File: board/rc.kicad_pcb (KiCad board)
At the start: 2 copper layers, 74 x 47.3 mm, 42 parts, among them IC1 A3909GLNTR-T, J1 Conn_01x24, J2 Conn_01x06, Q1 Q_NPN_BEC, Q2 Q_NPN_BEC, U1 ESP32-S3-MINI-1U, U2 TPS560430YDBVR, U3 XC6206PxxxMR, U4 XC6206PxxxMR

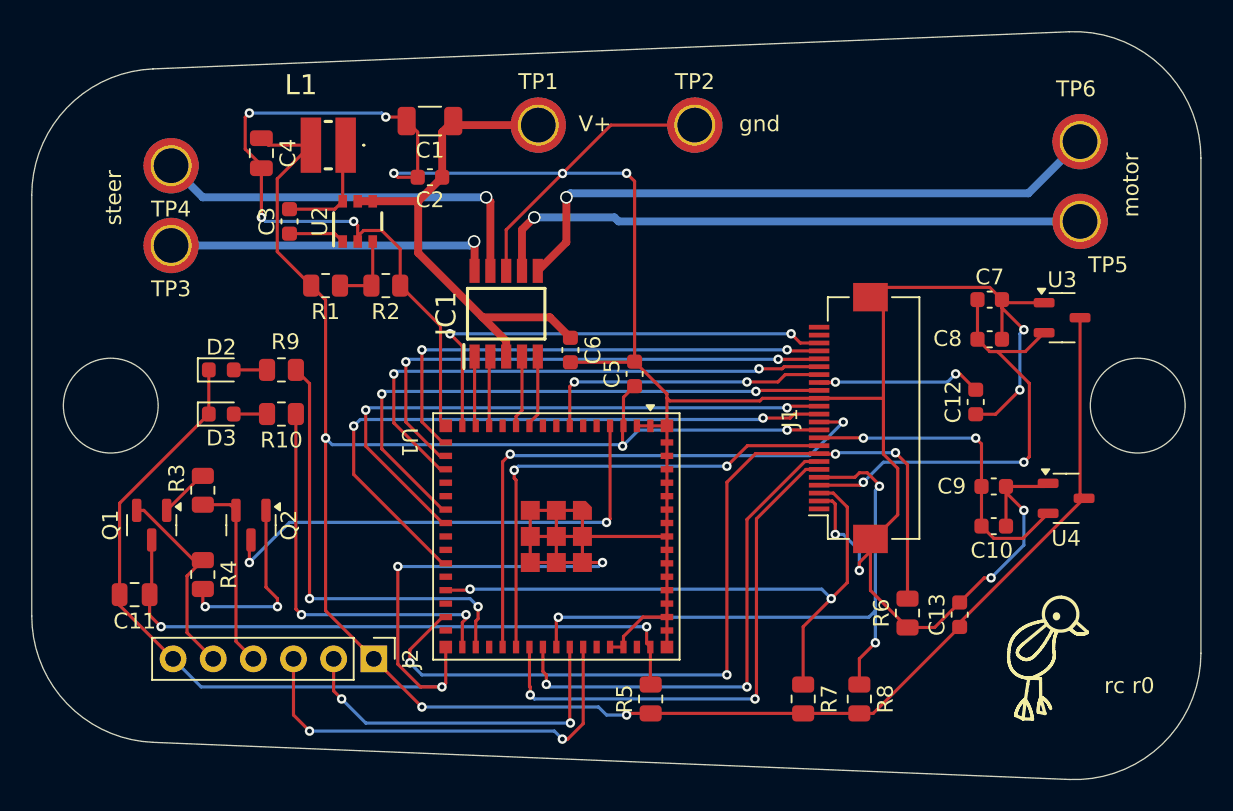
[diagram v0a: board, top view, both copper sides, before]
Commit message: added another motor driver, made mounting holes smaller, added cap for input voltage
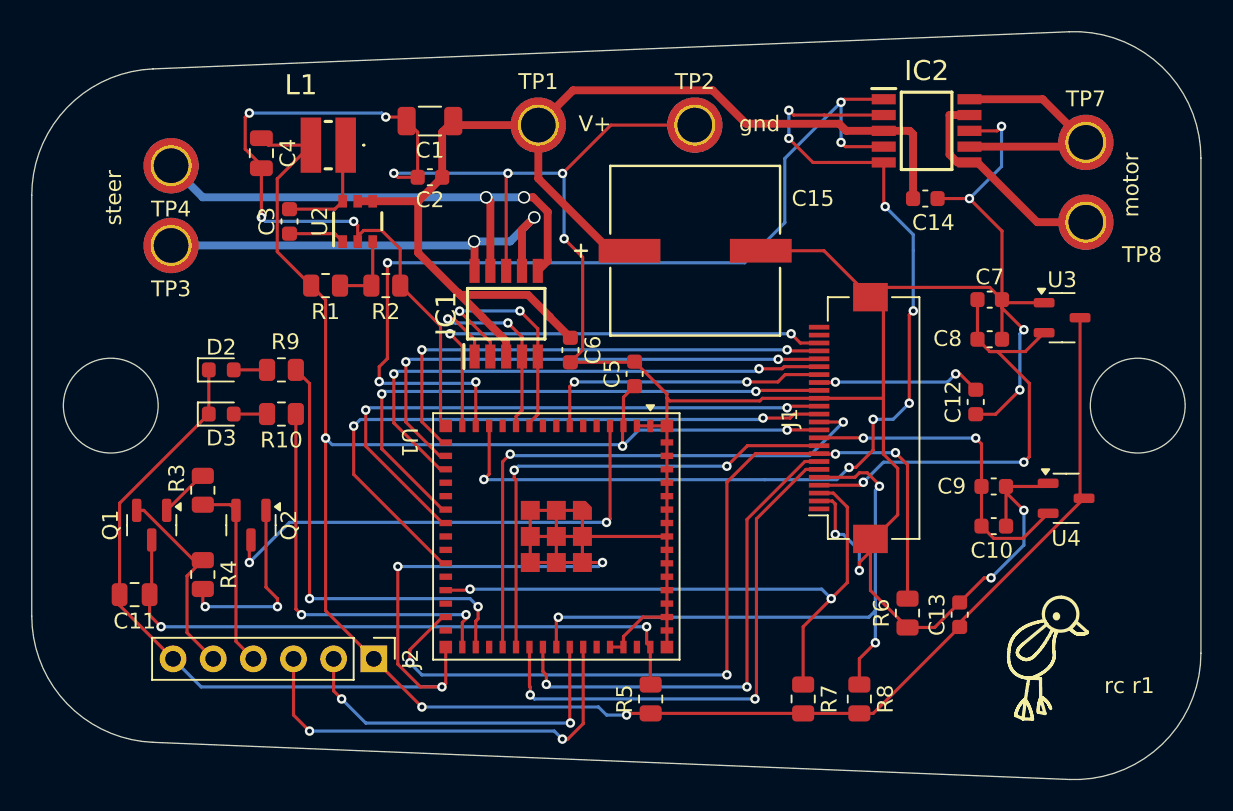
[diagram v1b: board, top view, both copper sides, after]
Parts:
- removed TP5, TP6: TestPoint, MountingHole:MountingHole_2.2mm_M2_ISO7380_Pad_TopBottom
- added C14: 0.1uF, Capacitor_SMD:C_0603_1608Metric, F.Cu at (169.9, 57.4)
- added C15: UCW1H221MNL1GS, footprints2:UCW1H221MNL1GS, F.Cu at (155.4, 60.7)
- added IC2: A3909GLNTR-T, footprints:SOP100P600X175-10N, F.Cu at (170.0, 53.1)
- added TP7: TestPoint, MountingHole:MountingHole_2.2mm_M2_ISO7380_Pad_TopBottom, F.Cu at (180.1, 53.8)
- added TP8: TestPoint, MountingHole:MountingHole_2.2mm_M2_ISO7380_Pad_TopBottom, F.Cu at (180.1, 58.9)
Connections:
- IC1 pad 1: /motor_a -> /steer_a
- IC1 pad 2: /motor_b -> /steer_b
- IC1 pad 6: Net-(IC1-OUT4) -> Net-(IC1-OUT2)
- IC1 pad 7: Net-(IC1-OUT3) -> Net-(IC1-OUT1)
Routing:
- net /motor_b: track 4.42 -> 64.3 mm, vias 0 -> 8
- net /motor_a: track 4.42 -> 60.3 mm, vias 0 -> 5
- net /V_IN: track 33.5 -> 76.7 mm
- net Net-(IC1-OUT4): track 39.4 -> 0.00 mm, vias 1 -> 0
- net Net-(IC1-OUT3): track 38.4 -> 0.00 mm, vias 1 -> 0
- net GND: track 300.2 -> 320.4 mm, vias 16 -> 19
- net Net-(IC2-OUT1): track 0.00 -> 16.0 mm
- net Net-(IC2-OUT2): track 0.00 -> 14.2 mm
- net /steer_b: track 4.60 -> 15.7 mm, vias 0 -> 2
- net /steer_a: track 4.54 -> 14.6 mm, vias 0 -> 2
- net Net-(IC1-OUT2): track 25.5 -> 33.8 mm, vias 1 -> 2
- net Net-(IC1-OUT1): track 21.2 -> 29.3 mm, vias 1 -> 2
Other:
- board text added: "rc r1"
- board text removed: "rc r0"
